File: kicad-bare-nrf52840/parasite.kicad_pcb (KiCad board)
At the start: 2 copper layers, 22 x 126.4 mm, 31 parts, among them Q1 MMBT3906, Q4 Q_Photo_NPN, SW1 B3U-1000P, U1 E73-2G4M08S1C, U2 SHTC3, Y1 32.768kHz

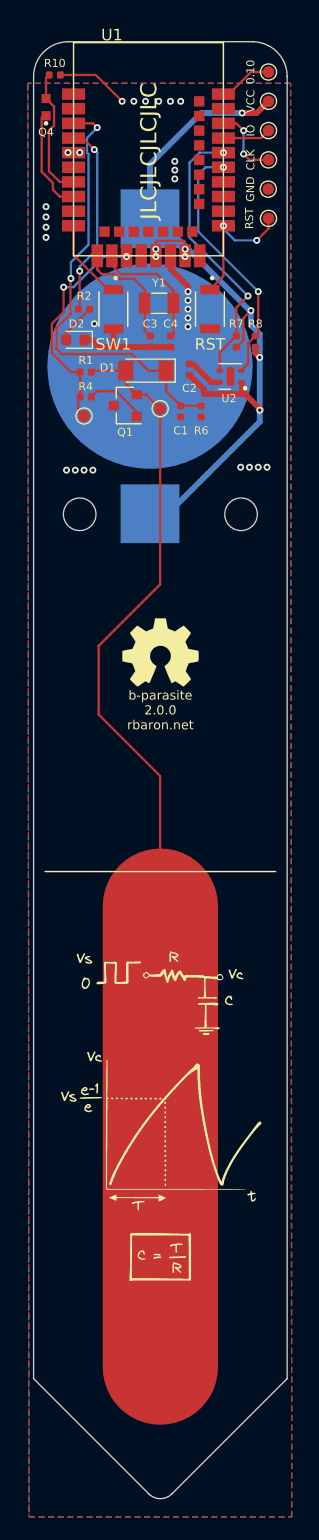
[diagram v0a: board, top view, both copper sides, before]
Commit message: feat: place bare MCU support circuitry and route critical analog networks
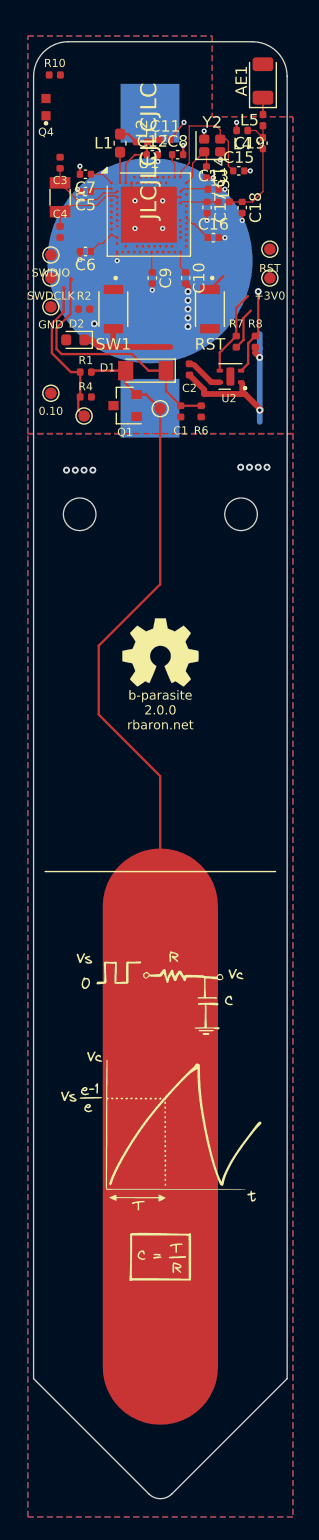
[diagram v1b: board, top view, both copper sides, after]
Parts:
- added AE1: 2450AT18B0100001E, Johanson_2450AT18x100, F.Cu at (76.9, 30.4)
- added C10: 100n, C_0402_1005Metric, F.Cu at (70.2, 47.5)
- added C11: 1u, C_0402_1005Metric, F.Cu at (68.4, 35.5)
- added C12: 47n, C_0402_1005Metric, F.Cu at (67.3, 36.8)
- added C13: 100p, C_0402_1005Metric, F.Cu at (72.6, 39.8)
- added C14: 12p, C_0402_1005Metric, F.Cu at (72.0, 38.3)
- added C15: 12p, C_0402_1005Metric, F.Cu at (74.8, 38.2)
- added C16: 820p, C_0402_1005Metric, F.Cu at (72.6, 44.0)
- added C17: 0.8p, C_0402_1005Metric, F.Cu at (72.0, 41.4)
- added C18: 0.5p, C_0402_1005Metric, F.Cu at (75.1, 41.4)
- added C19: 1.2p, C_0402_1005Metric, F.Cu at (76.9, 35.8)
- added C5: 100n, C_0402_1005Metric, F.Cu at (61.5, 40.0)
- added C6: 4.7u, C_0402_1005Metric, F.Cu at (61.5, 45.2)
- added C7: 1u, C_0402_1005Metric, F.Cu at (61.5, 38.5)
- added C8: 100n, C_0402_1005Metric, F.Cu at (69.5, 36.8)
- added C9: 100n, C_0402_1005Metric, F.Cu at (67.3, 47.5)
- added L1: 10u, L_0603_1608Metric, F.Cu at (64.5, 35.8)
- added L2: 15n, L_0402_1005Metric, F.Cu at (66.4, 35.7)
- added L3: 4.7n, L_0402_1005Metric, F.Cu at (73.5, 40.9)
- added L4: 2.7n, L_0402_1005Metric, F.Cu at (75.1, 34.7)
- added L5: 3.3n, L_0402_1005Metric, F.Cu at (76.9, 33.8)
- added Y2: 32MHz, Crystal_SMD_2016-4Pin_2.0x1.6mm, F.Cu at (72.5, 36.0)
- TP1: value IO -> SWDIO
- TP2: value CLK -> SWDCLK
- TP7: value VCC -> +3V0
- U1: value E73-2G4M08S1C -> nRF52840-QIAA; footprint snapeda:E73-2G4M08S1C -> Nordic_AQFN-73-1EP_7x7mm_P0.5mm
- moved TP8 33.7 mm to (58.5, 57.5), turned to 0 degrees
- moved TP1 21.7 mm to (58.5, 45.5), turned to 0 degrees
- moved TP2 21.5 mm to (58.5, 47.5), turned to 0 degrees
- moved TP3 21.4 mm to (58.5, 50.0), turned to 0 degrees
- moved C3 17.4 mm to (59.3, 37.5), turned to -90 degrees
- moved TP7 15.3 mm to (77.5, 47.5), turned to 0 degrees
- moved C4 13.5 mm to (59.3, 43.5)
- moved Y1 12.6 mm to (59.3, 40.5), turned to -90 degrees
- moved BT1 9.16 mm to (67.1, 46.0)
- moved U1 5.43 mm to (67.0, 42.0)
- moved TP4 2.67 mm to (77.5, 45.0), turned to 0 degrees
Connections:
- C3 pad 2: Net-(U1B-P0.00/XL1) -> XL1
- C4 pad 1: Net-(U1B-P0.01/XL2) -> XL2
- U2 pad 5: unconnected-(U2-NC-Pad5) -> (no net)
- Y1 pad 1: Net-(U1B-P0.01/XL2) -> XL2
- Y1 pad 2: Net-(U1B-P0.00/XL1) -> XL1
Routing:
- net +3V0: track 76.5 -> 31.9 mm, vias 8 -> 2
- net SDA: track 24.5 -> 7.50 mm, vias 2 -> 0
- net LED: track 16.9 -> 0.15 mm, vias 2 -> 0
- net SENS_OUT: track 38.5 -> 22.2 mm, vias 2 -> 0
- net SCL: track 22.2 -> 7.48 mm, vias 2 -> 1
- net XC2: track 0.00 -> 11.9 mm
- net PHOTO_OUT: track 11.5 -> 0.00 mm
- net Net-(U1B-P0.01/XL2): track 11.1 -> 0.00 mm
- net RST: track 11.9 -> 1.65 mm, vias 2 -> 0
- net Net-(U1B-P0.00/XL1): track 10.2 -> 0.00 mm
- net PHOTO_V: track 8.72 -> 0.00 mm
- net XL1: track 0.00 -> 7.11 mm
- net RF_50: track 0.00 -> 7.01 mm
- net XL2: track 0.00 -> 6.84 mm
- net BTN1: track 7.22 -> 0.45 mm
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- added copper zone on In1.Cu, net GND
- added copper zone on In2.Cu, net GND
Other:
- copper layers 2 -> 4
- rule pad_to_mask_clearance: 0.051 -> 0
- rule solder_mask_min_width: 0.25 -> 0.075

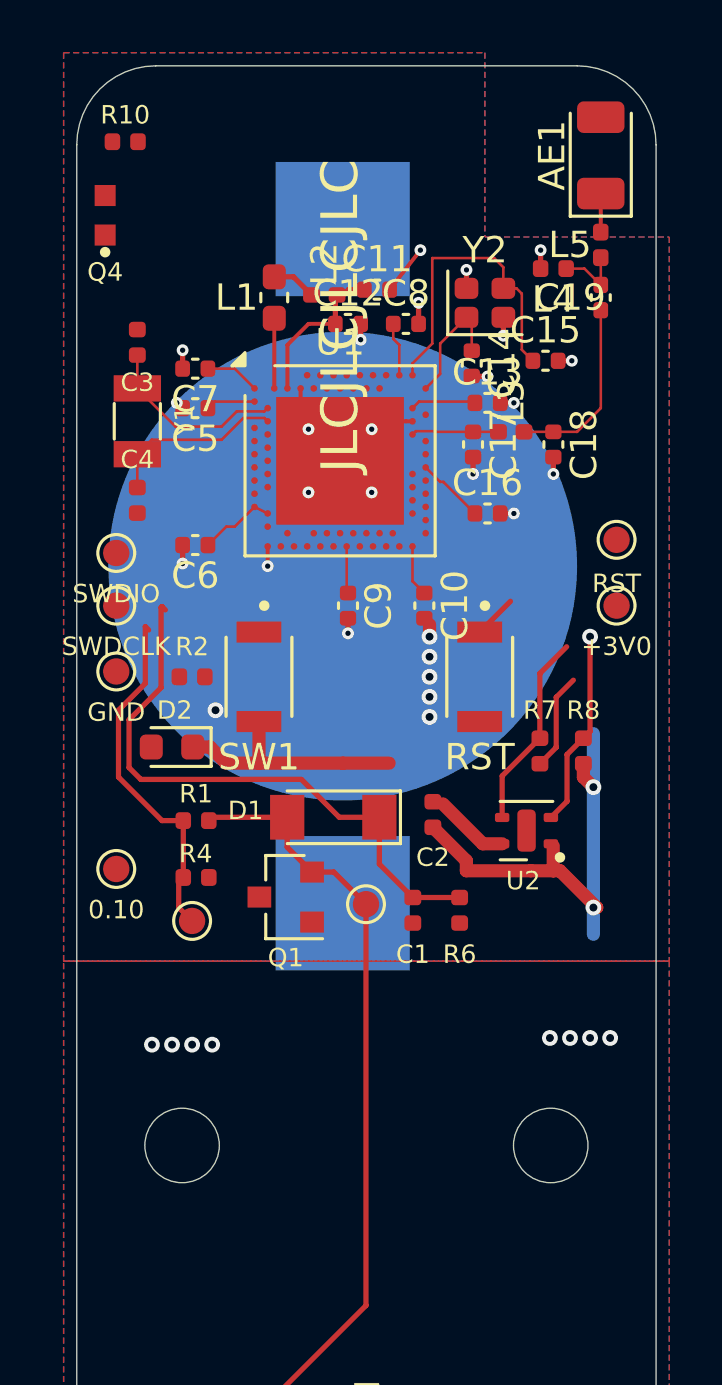
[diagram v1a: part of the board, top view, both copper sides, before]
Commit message: feat: add Tag-Connect SWD port and free MCU fanout with compact battery contacts
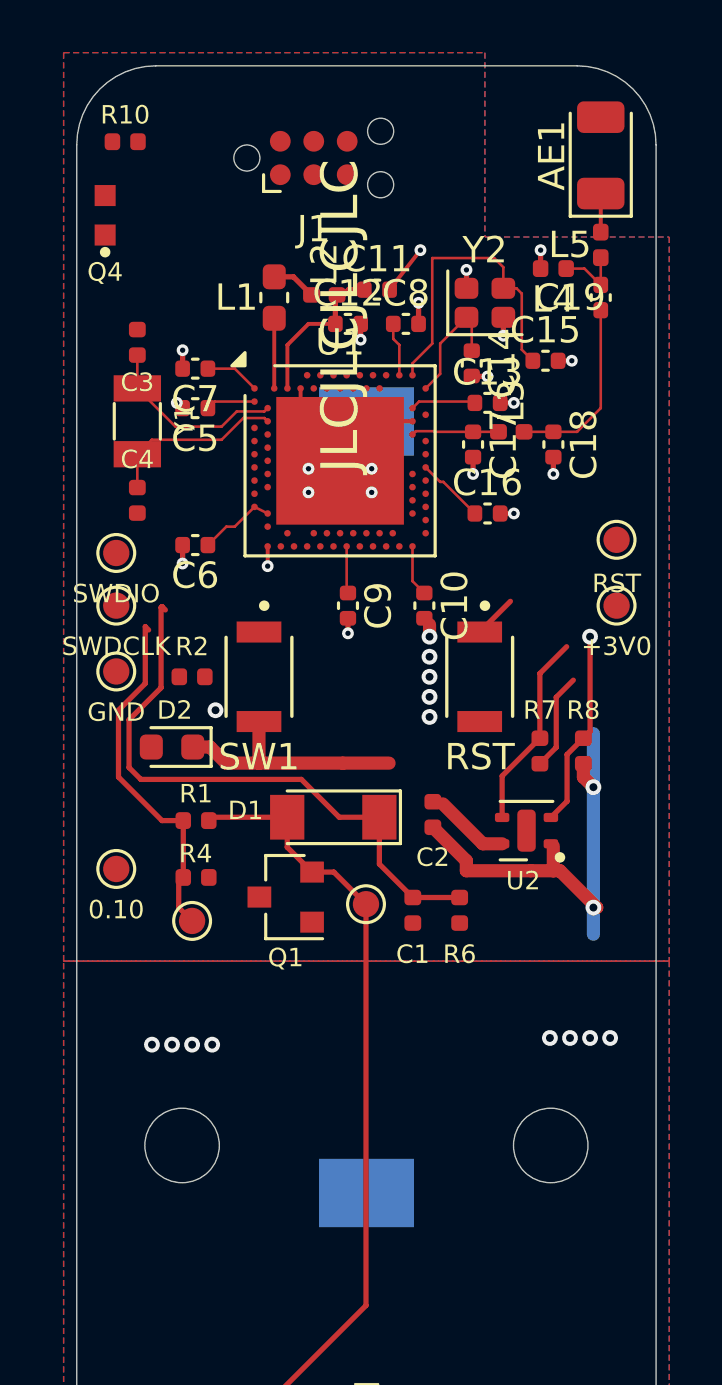
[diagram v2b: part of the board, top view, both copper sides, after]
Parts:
- added J1: TC2030-SWD, Connector:Tag-Connect_TC2030-IDC-NL_2x03_P1.27mm_Vertical, F.Cu at (66.0, 30.5)
- BT1: footprint kicad:BatteryHolder_Keystone_3002_1x2032 -> Battery:BatteryHolder_Keystone_1060_1x2032
- moved BT1 9.20 mm to (68.0, 55.2)

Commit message: checkpoint: before via-in-pad MCU fanout refinement
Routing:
- net +3V0: track 31.9 -> 94.1 mm, vias 2 -> 6
- net SWDCLK: track 0.00 -> 39.1 mm, vias 0 -> 3
- net SWDIO: track 0.00 -> 38.9 mm, vias 0 -> 3
- net 0.10: track 0.00 -> 26.6 mm, vias 0 -> 2
- net RST: track 1.65 -> 27.1 mm, vias 0 -> 2
- net PHOTO_OUT: track 0.00 -> 14.7 mm, vias 0 -> 2
- net SCL: track 7.48 -> 21.9 mm, vias 1 -> 2
- net PHOTO_V: track 0.00 -> 10.8 mm, vias 0 -> 2
- net SDA: track 7.50 -> 17.5 mm, vias 0 -> 2
- net DEC4_6: track 6.03 -> 13.7 mm, vias 0 -> 2
- net Net-(Q1-B): track 0.00 -> 4.62 mm
- net Net-(D2-A): track 0.00 -> 3.51 mm
- net XL2: track 6.84 -> 7.61 mm

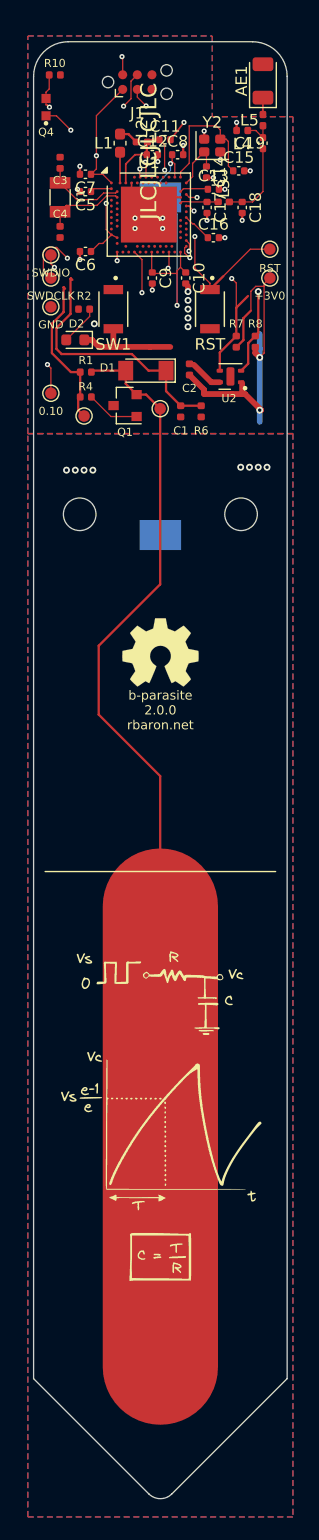
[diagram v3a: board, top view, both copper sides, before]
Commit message: feat: escape inner MCU pads with filled vias and relocate battery below MCU
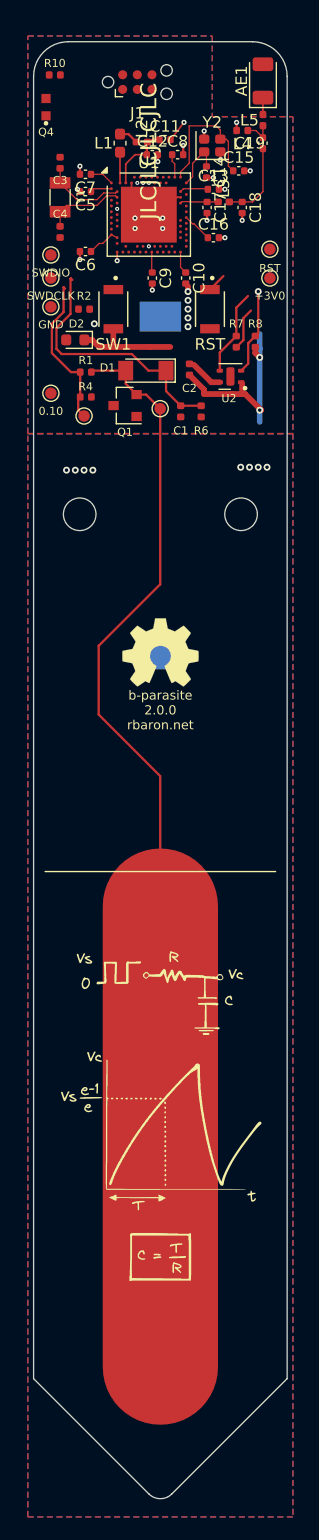
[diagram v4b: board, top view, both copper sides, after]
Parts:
- moved BT1 10.3 mm to (68.0, 65.5)
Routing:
- net +3V0: track 94.1 -> 31.9 mm, vias 6 -> 2
- net SWDCLK: track 39.1 -> 0.00 mm, vias 3 -> 0
- net SWDIO: track 38.9 -> 0.00 mm, vias 3 -> 0
- net 0.10: track 26.6 -> 0.00 mm, vias 2 -> 0
- net RST: track 27.1 -> 1.65 mm, vias 2 -> 1
- net PHOTO_OUT: track 14.7 -> 0.00 mm, vias 2 -> 0
- net SCL: track 21.9 -> 7.48 mm, vias 2 -> 1
- net PHOTO_V: track 10.8 -> 0.00 mm, vias 2 -> 0
- net SDA: track 17.5 -> 7.50 mm, vias 2 -> 0
- net DEC4_6: track 13.7 -> 6.03 mm, vias 2 -> 0
- net Net-(Q1-B): track 4.62 -> 0.00 mm
- net Net-(D2-A): track 3.51 -> 0.00 mm
- net XL2: track 7.61 -> 6.84 mm
- net SENS_OUT: track 22.5 -> 22.2 mm, vias 0 -> 1
- net PWM: vias 0 -> 1
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
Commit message: feat: complete four-layer routing and clarify schematic and SWD markings
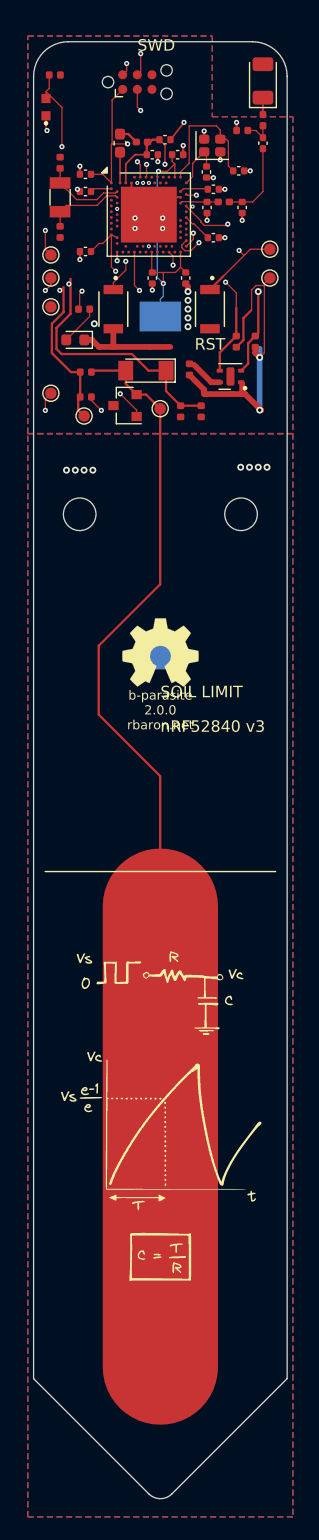
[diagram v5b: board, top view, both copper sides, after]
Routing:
- net +3V0: track 31.9 -> 94.6 mm, vias 2 -> 6
- net SWDCLK: track 0.00 -> 47.6 mm, vias 0 -> 3
- net 0.10: track 0.00 -> 40.6 mm, vias 0 -> 2
- net SWDIO: track 0.00 -> 39.3 mm, vias 0 -> 3
- net RST: track 1.65 -> 32.2 mm, vias 1 -> 3
- net SCL: track 7.48 -> 25.1 mm, vias 1 -> 2
- net PHOTO_OUT: track 0.00 -> 16.8 mm, vias 0 -> 2
- net LED: track 0.15 -> 14.3 mm, vias 1 -> 2
- net SENS_OUT: track 22.2 -> 36.2 mm, vias 1 -> 2
- net PHOTO_V: track 0.00 -> 11.7 mm, vias 0 -> 2
- net PWM: track 13.6 -> 24.9 mm, vias 1 -> 2
- net BTN1: track 0.45 -> 10.6 mm, vias 1 -> 2
- net SDA: track 7.50 -> 15.1 mm, vias 0 -> 2
- net DEC4_6: track 6.03 -> 13.1 mm, vias 0 -> 2
- net Net-(Q1-B): track 0.00 -> 6.34 mm, vias 0 -> 2
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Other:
- board text added: "SOIL LIMIT"
- board text added: "SWD"
- board text added: "nRF52840 v3"
- board text removed: "JLCJLCJLCJLC"

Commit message: feat: reconcile PCB library links and validate complete schematic parity
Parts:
- AE1: footprint Johanson_2450AT18x100 -> RF_Antenna:Johanson_2450AT18x100
- C10, C11, C12, C13, C14, C15, C16, C17, C18, C19, C5, C6, C7, C8, C9: footprint C_0402_1005Metric -> Capacitor_SMD:C_0402_1005Metric
- L1: footprint L_0603_1608Metric -> Inductor_SMD:L_0603_1608Metric
- L2, L3, L4, L5: footprint L_0402_1005Metric -> Inductor_SMD:L_0402_1005Metric
- U1: footprint Nordic_AQFN-73-1EP_7x7mm_P0.5mm -> Package_DFN_QFN:Nordic_AQFN-73-1EP_7x7mm_P0.5mm
- Y2: footprint Crystal_SMD_2016-4Pin_2.0x1.6mm -> Crystal:Crystal_SMD_2016-4Pin_2.0x1.6mm
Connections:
- AE1 pad 2: (no net) -> unconnected-(AE1-PCB_Trace-Pad2)
- J1 pad 6: (no net) -> unconnected-(J1-Pin_6-Pad6)
- U1 pad A14: (no net) -> unconnected-(U1-P1.15-PadA14)
- U1 pad A16: (no net) -> unconnected-(U1-P1.13-PadA16)
- U1 pad A18: (no net) -> unconnected-(U1-DEC2-PadA18)
- U1 pad A20: (no net) -> unconnected-(U1-P1.10-PadA20)
- U1 pad A8: (no net) -> unconnected-(U1-AIN7/P0.31-PadA8)
- U1 pad AB2: (no net) -> unconnected-(U1-DCCH-PadAB2)
- U1 pad AC11: (no net) -> unconnected-(U1-P0.16-PadAC11)
- U1 pad AC15: (no net) -> unconnected-(U1-P0.19-PadAC15)
- U1 pad AC17: (no net) -> unconnected-(U1-P0.21-PadAC17)
- U1 pad AC19: (no net) -> unconnected-(U1-P0.23-PadAC19)
- U1 pad AC21: (no net) -> unconnected-(U1-P0.25-PadAC21)
- U1 pad AC5: (no net) -> unconnected-(U1-DECUSB-PadAC5)
- U1 pad AC9: (no net) -> unconnected-(U1-P0.14-PadAC9)
- U1 pad AD10: (no net) -> unconnected-(U1-P0.15-PadAD10)
- U1 pad AD12: (no net) -> unconnected-(U1-P0.17-PadAD12)
- U1 pad AD16: (no net) -> unconnected-(U1-P0.20-PadAD16)
- U1 pad AD18: (no net) -> unconnected-(U1-P0.22-PadAD18)
- U1 pad AD22: (no net) -> unconnected-(U1-TRACEDATA0/P1.00-PadAD22)
- U1 pad AD4: (no net) -> unconnected-(U1-D--PadAD4)
- U1 pad AD6: (no net) -> unconnected-(U1-D+-PadAD6)
- U1 pad B15: (no net) -> unconnected-(U1-P1.14-PadB15)
- U1 pad B17: (no net) -> unconnected-(U1-P1.12-PadB17)
- U1 pad B19: (no net) -> unconnected-(U1-P1.11-PadB19)
- U1 pad G1: (no net) -> unconnected-(U1-P0.26-PadG1)
- U1 pad H2: (no net) -> unconnected-(U1-P0.27-PadH2)
- U1 pad J1: (no net) -> unconnected-(U1-AIN2/P0.04-PadJ1)
- U1 pad L1: (no net) -> unconnected-(U1-P0.06-PadL1)
- U1 pad L24: (no net) -> unconnected-(U1-NFC1/P0.09-PadL24)
- U1 pad M2: (no net) -> unconnected-(U1-TRACECLK/P0.07-PadM2)
- U1 pad N1: (no net) -> unconnected-(U1-P0.08-PadN1)
- U1 pad P2: (no net) -> unconnected-(U1-P1.08-PadP2)
- U1 pad P23: (no net) -> unconnected-(U1-P1.07-PadP23)
- U1 pad R1: (no net) -> unconnected-(U1-TRACEDATA3/P1.09-PadR1)
- U1 pad R24: (no net) -> unconnected-(U1-P1.06-PadR24)
- U1 pad T2: (no net) -> unconnected-(U1-TRACEDATA2/P0.11-PadT2)
- U1 pad T23: (no net) -> unconnected-(U1-P1.05-PadT23)
- U1 pad U1: (no net) -> unconnected-(U1-TRACEDATA1/P0.12-PadU1)
- U1 pad U24: (no net) -> unconnected-(U1-P1.04-PadU24)
- U1 pad V23: (no net) -> unconnected-(U1-P1.03-PadV23)
- U1 pad W24: (no net) -> unconnected-(U1-P1.02-PadW24)
- U1 pad Y23: (no net) -> unconnected-(U1-P1.01-PadY23)
- U2 pad 5: (no net) -> unconnected-(U2-NC-Pad5)
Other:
- rule solder_mask_min_width: 0.075 -> 0.1
- board text added: "b-parasite rbaron.net"
- board text removed: "b-parasite 2.0.0 rbaron.net"

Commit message: feat: resolve KiCad warnings and align stackup and sourcing for fabrication
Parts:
- added TP9: SOIL_ELECTRODE, b-parasite:Soil_Electrode_Endpoint_Covered, F.Cu at (68.0, 142.0)
- BT1: footprint Battery:BatteryHolder_Keystone_1060_1x2032 -> b-parasite:BatteryHolder_Keystone_1060_NoBodySilk
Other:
- board text added: "Chris Tolleson"
- board text removed: "b-parasite rbaron.net"
